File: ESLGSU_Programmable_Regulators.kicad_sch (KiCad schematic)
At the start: 0 parts

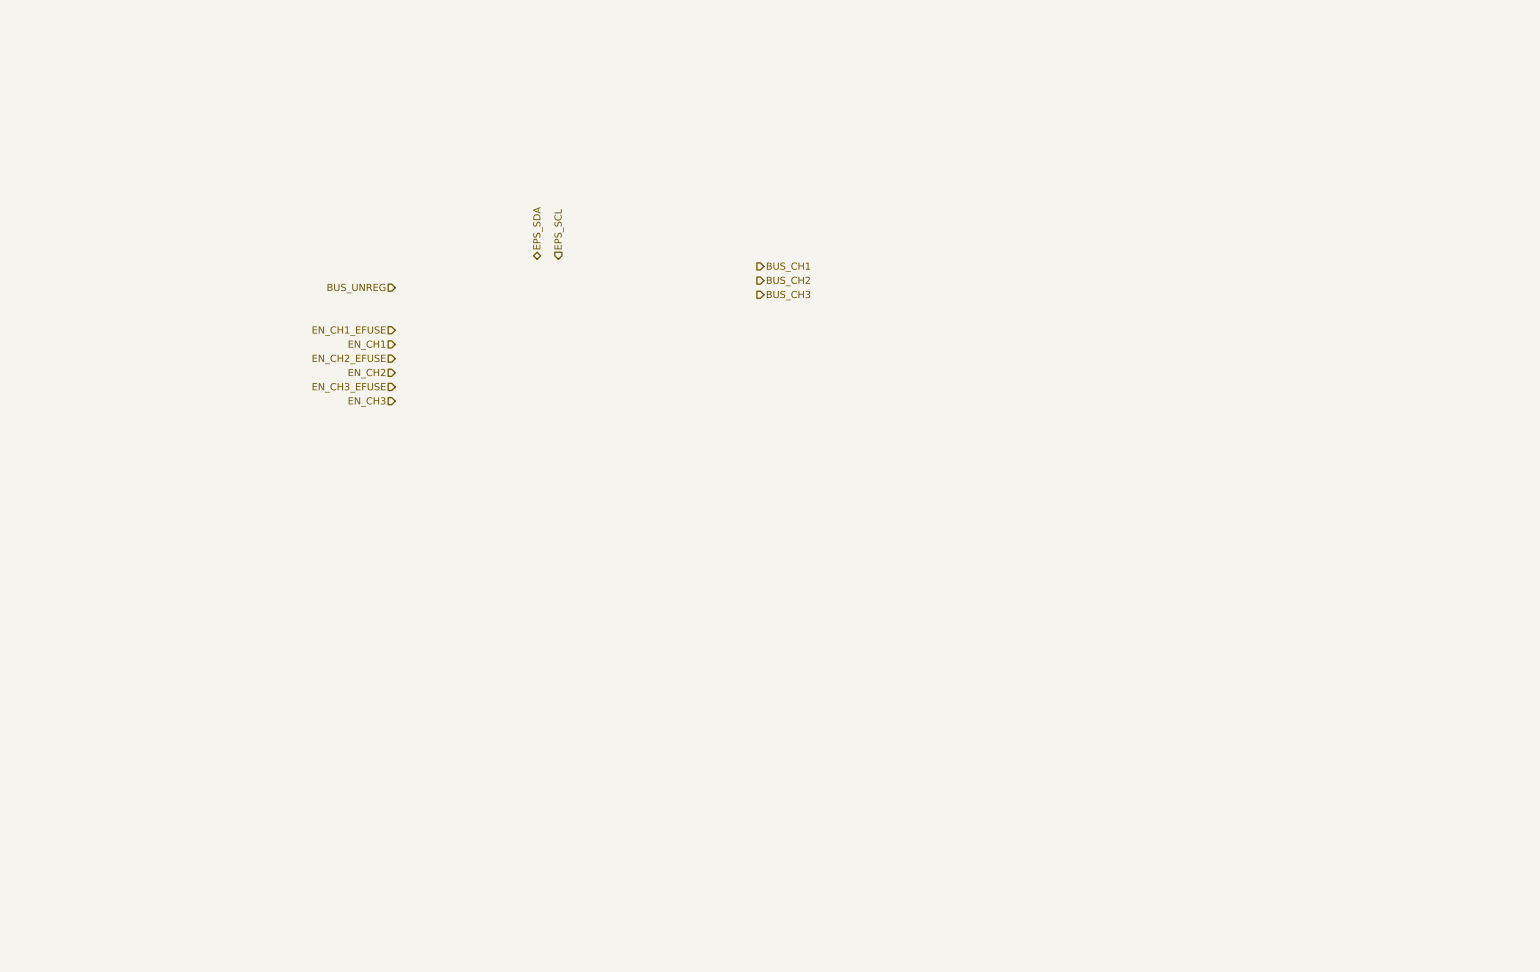
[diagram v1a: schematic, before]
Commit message: Additional power regulation work
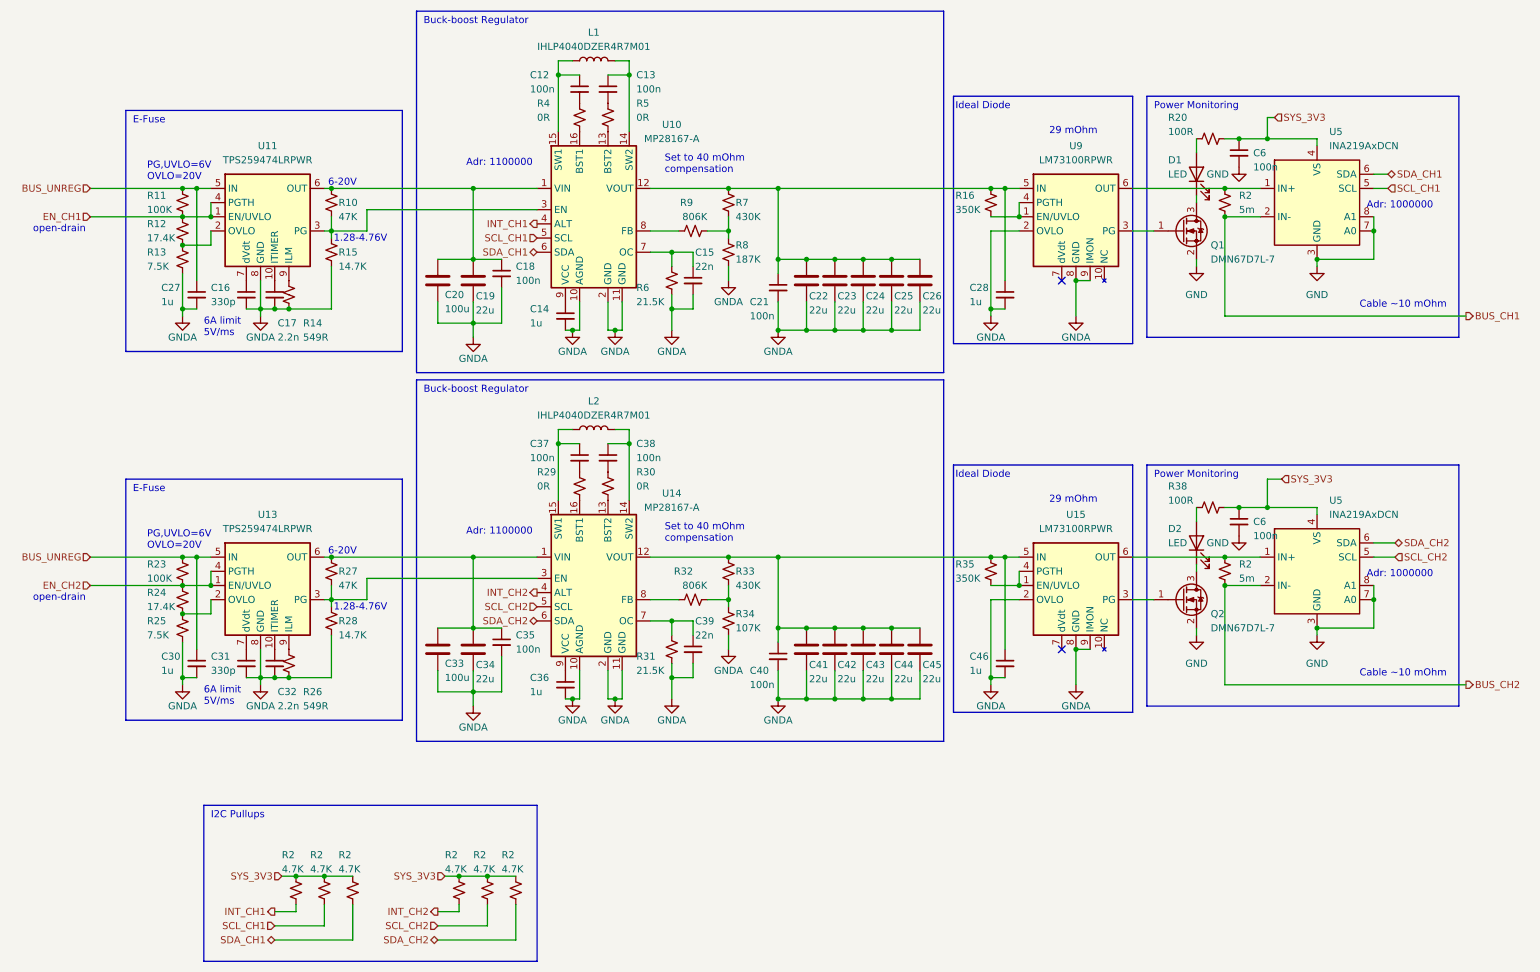
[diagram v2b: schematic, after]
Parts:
- added C12, C13, C18, C21, C35, C37, C38, C40, C6 (x2): 100n, Capacitor_SMD:C_0603_1608Metric, symbol Device:C_Small
- added C14, C27, C28, C30, C36, C46: 1u, Capacitor_SMD:C_0603_1608Metric, symbol Device:C_Small
- added C15, C39: 22n, Capacitor_SMD:C_0603_1608Metric, symbol Device:C_Small
- added C16, C31: 330p, Capacitor_SMD:C_0603_1608Metric, symbol Device:C_Small
- added C17, C32: 2.2n, Capacitor_SMD:C_0603_1608Metric, symbol Device:C_Small
- added C19, C22, C23, C24, C25, C26, C34, C41, C42, C43, C44, C45: 22u, Capacitor_SMD:C_0805_2012Metric, symbol Device:C
- added C20, C33: 100u, Capacitor_SMD:CP_Elec_6.3x7.7, symbol Device:C
- added D1, D2: LED, LED_SMD:LED_0603_1608Metric, symbol Device:LED
- added L1, L2: IHLP4040DZER4R7M01, Inductor_SMD:L_Vishay_IHLP-4040, symbol Device:L
- added Q1, Q2: DMN67D7L-7, Package_TO_SOT_SMD:SOT-323_SC-70, symbol Transistor_FET:DMN67D7L
- added R10, R27: 47K, Resistor_SMD:R_0603_1608Metric, symbol Device:R_Small_US
- added R11, R23: 100K, Resistor_SMD:R_0603_1608Metric, symbol Device:R_Small_US
- added R12, R24: 17.4K, Resistor_SMD:R_0603_1608Metric, symbol Device:R_Small_US
- added R13, R25: 7.5K, Resistor_SMD:R_0603_1608Metric, symbol Device:R_Small_US
- added R14, R26: 549R, Resistor_SMD:R_0603_1608Metric, symbol Device:R_Small_US
- added R15, R28: 14.7K, Resistor_SMD:R_0603_1608Metric, symbol Device:R_Small_US
- added R16, R35: 350K, Resistor_SMD:R_0603_1608Metric, symbol Device:R_Small_US
- added R2 (x2): 5m, Resistor_SMD:R_0603_1608Metric, symbol Device:R_Small_US
- added R2 (x6): 4.7K, Resistor_SMD:R_0603_1608Metric, symbol Device:R_Small_US
- added R20, R38: 100R, Resistor_SMD:R_0603_1608Metric, symbol Device:R_Small_US
- added R29, R30, R4, R5: 0R, Resistor_SMD:R_0603_1608Metric, symbol Device:R_Small_US
- added R31, R6: 21.5K, Resistor_SMD:R_0603_1608Metric, symbol Device:R_Small_US
- added R32, R9: 806K, Resistor_SMD:R_0603_1608Metric, symbol Device:R_Small_US
- added R33, R7: 430K, Resistor_SMD:R_0603_1608Metric, symbol Device:R_Small_US
- added R34: 107K, Resistor_SMD:R_0603_1608Metric, symbol Device:R_Small_US
- added R8: 187K, Resistor_SMD:R_0603_1608Metric, symbol Device:R_Small_US
- added U10, U14: MP28167-A, ESLGSU_Parts_Lib:QFN-16-MP28167, symbol ESLGSU_Parts_Lib:MP28167-A
- added U11, U13: TPS259474LRPWR, ESLGSU_Parts_Lib:VQFN-HR, symbol ESLGSU_Parts_Lib:TPS259474ARPWR
- added U15, U9: LM73100RPWR, ESLGSU_Parts_Lib:VQFN-HR, symbol ESLGSU_Parts_Lib:LM73100
- added U5 (x2): INA219AxDCN, Package_TO_SOT_SMD:SOT-23-8, symbol Sensor_Energy:INA219AxDCN
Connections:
- net BUS_CH1: now also R2.2, U5.2 (IN-)
- net BUS_CH2: now also R2.2, U5.2 (IN-)
- net BUS_UNREG: now also C27.1, C30.1, R11.1, R23.1, U11.5 (IN), U13.5 (IN)
- net EN_CH1: now also R11.2, R12.1, U11.1 (EN/UVLO), U11.4 (PGTH)
- net EN_CH2: now also R23.2, R24.1, U13.1 (EN/UVLO), U13.4 (PGTH)
- new net: D1.1 (K), Q1.3 (D)
- new net: D1.2 (A), R20.2
- new net: C21.1, C22.1, C23.1, C24.1, C25.1, C26.1, C28.1, R16.1, R7.1, U10.12 (VOUT), U9.5 (IN)
- new net: C17.1, U11.10 (ITIMER)
- new net: R12.2, R13.1, U11.2 (OVLO)
- new net: R10.2, R15.1, U10.3 (EN), U11.3 (PG)
- new net: C18.1, C19.1, C20.1, R10.1, U10.1 (VIN), U11.6 (OUT)
- new net: C16.1, U11.7 (dVdt)
- new net: R14.1, U11.9 (ILM)
- new net: C40.1, C41.1, C42.1, C43.1, C44.1, C45.1, C46.1, R33.1, R35.1, U14.12 (VOUT), U15.5 (IN)
- new net: R35.2, U15.1 (EN/UVLO), U15.4 (PGTH)
- new net: Q2.1 (G), U15.3 (PG)
- new net: R2.1, U15.6 (OUT), U5.1 (IN+)
- new net: C33.1, C34.1, C35.1, R27.1, U13.6 (OUT), U14.1 (VIN)
- new net: C38.1, L2.2, U14.14 (SW2)
- new net: C38.2, R30.1
- new net: C14.1, U10.9 (VCC)
- new net: R24.2, R25.1, U13.2 (OVLO)
- new net: R32.2, R33.2, R34.1
- new net: R7.2, R8.1, R9.2
- new net: R27.2, R28.1, U13.3 (PG), U14.3 (EN)
- new net: R16.2, U9.1 (EN/UVLO), U9.4 (PGTH)
- new net: C13.2, R5.1
- new net: R5.2, U10.13 (BST2)
- new net: C13.1, L1.2, U10.14 (SW2)
- new net: C12.1, L1.1, U10.15 (SW1)
- new net: R4.2, U10.16 (BST1)
- new net: C15.1, R6.1, U10.7 (OC)
- new net: R9.1, U10.8 (FB)
- new net: C37.1, L2.1, U14.15 (SW1)
- new net: C37.2, R29.1
- new net: D2.1 (K), Q2.3 (D)
- new net: D2.2 (A), R38.2
- new net: R32.1, U14.8 (FB)
- new net: R26.1, U13.9 (ILM)
- new net: C36.1, U14.9 (VCC)
- new net: C39.1, R31.1, U14.7 (OC)
- new net: R2.1, U5.1 (IN+), U9.6 (OUT)
- new net: R30.2, U14.13 (BST2)
- new net: C32.1, U13.10 (ITIMER)
- new net: R29.2, U14.16 (BST1)
- new net: Q1.1 (G), U9.3 (PG)
- new net: C31.1, U13.7 (dVdt)
- new net: C12.2, R4.1
- new net GND: C6.2, C6.2, Q1.2 (S), Q2.2 (S), U5.3 (GND), U5.3 (GND), U5.7 (A0), U5.7 (A0), U5.8 (A1), U5.8 (A1)
- new net GNDA: C14.2, C15.2, C16.2, C17.2, C18.2, C19.2, C20.2, C21.2, C22.2, C23.2, C24.2, C25.2, C26.2, C27.2, C28.2, C30.2, C31.2, C32.2, C33.2, C34.2, C35.2, C36.2, C39.2, C40.2, C41.2, C42.2, C43.2, C44.2, C45.2, C46.2, R13.2, R14.2, R15.2, R25.2, R26.2, R28.2, R31.2, R34.2, R6.2, R8.2, U10.10 (AGND), U10.11 (GND), U10.2 (GND), U11.8 (GND), U13.8 (GND), U14.10 (AGND), U14.11 (GND), U14.2 (GND), U15.2 (OVLO), U15.8 (GND), U15.9 (IMON), U9.2 (OVLO), U9.8 (GND), U9.9 (IMON)
- new net INT_CH1: R2.2, U10.4 (ALT)
- new net INT_CH2: R2.2, U14.4 (ALT)
- new net SCL_CH1: R2.2, U10.5 (SCL), U5.5 (SCL)
- new net SCL_CH2: R2.2, U14.5 (SCL), U5.5 (SCL)
- new net SDA_CH1: R2.2, U10.6 (SDA), U5.6 (SDA)
- new net SDA_CH2: R2.2, U14.6 (SDA), U5.6 (SDA)
- new net SYS_3V3: C6.1, C6.1, R2.1, R2.1, R2.1, R2.1, R2.1, R2.1, R20.1, R38.1, U5.4 (VS), U5.4 (VS)
- no-connect marks 0 -> 2
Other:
- note added: "1.28-4.76V"
- note added: "29 mOhm"
- note added: "6-20V"
- note added: "6A limit 5V/ms"
- note added: "Adr: 1000000"
- note added: "Adr: 1100000"
- note added: "Buck-boost Regulator"
- note added: "Cable ~10 mOhm"
- note added: "E-Fuse"
- note added: "I2C Pullups"
- note added: "Ideal Diode"
- note added: "PG,UVLO=6V OVLO=20V"
- note added: "Power Monitoring"
- note added: "Set to 40 mOhm compensation"
- note added: "open-drain"

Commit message: Added 5v/3V3 regulators and mux
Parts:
- added R87 (x2): 47K, Resistor_SMD:R_0603_1608Metric, symbol Device:R_Small_US
- added TP1 (x6): TestPoint, TestPoint:TestPoint_Pad_D2.0mm, symbol Connector:TestPoint
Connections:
- net BUS_CH1: now also TP1.1
- net BUS_CH2: now also TP1.1
- net at D1.2 (A), R20.2: now also R87.1
- net at C21.1, C22.1, C23.1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: now also TP1.1
- net at C18.1, C19.1, C20.1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: now also TP1.1
- net at C40.1, C41.1, C42.1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: now also TP1.1
- net at Q2.1 (G), U15.3 (PG): now also R87.2
- net at C33.1, C34.1, C35.1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: now also TP1.1
- net at D2.2 (A), R38.2: now also R87.1
- net at Q1.1 (G), U9.3 (PG): now also R87.2

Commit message: uC Interface work
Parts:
- Q1, Q2: footprint Package_TO_SOT_SMD:SOT-323_SC-70 -> Package_TO_SOT_SMD:SOT-23
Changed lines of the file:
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@@
     )
   )
-  (symbol (lib_id "ESLGSU_Parts_Lib:LM73100") (at 203.2 121.92 0) (unit 1)
+  (symbol (lib_id "ESLGSU_Parts_Lib:LM73100") (at 203.2 120.65 0) (unit 1)
     (in_bom yes) (on_board yes) (dnp no) (fields_autoplaced)
-    (property "Reference" "U15" (at 203.2 109.22 0)
-      (effects (font (size 1.27 1.27)))
-    )
-    (property "Value" "LM73100RPWR" (at 203.2 111.76 0)
-      (effects (font (size 1.27 1.27)))
-    )
-    (property "Footprint" "ESLGSU_Parts_Lib:VQFN-HR" (at 201.93 140.97 0)
-      (effects (font (size 1.27 1.27)) hide)
-    )
-    (property "Datasheet" "" (at 203.2 121.92 0)
+    (property "Reference" "U15" (at 203.2 107.95 0)
+      (effects (font (size 1.27 1.27)))
+    )
+    (property "Value" "LM73100RPWR" (at 203.2 110.49 0)
+      (effects (font (size 1.27 1.27)))
+    )
+    (property "Footprint" "ESLGSU_Parts_Lib:VQFN-HR" (at 201.93 139.7 0)
+      (effects (font (size 1.27 1.27)) hide)
+    )
+    (property "Datasheet" "" (at 203.2 120.65 0)
       (effects (font (size 1.27 1.27)) hide)
     )
@@
       (effects (font (size 1.27 1.27)) (justify left))
     )
-    (property "Footprint" "Package_TO_SOT_SMD:SOT-323_SC-70" (at 227.33 126.365 0)
+    (property "Footprint" "Package_TO_SOT_SMD:SOT-23" (at 227.33 126.365 0)
       (effects (font (size 1.27 1.27) italic) (justify left) hide)
     )
@@
       (effects (font (size 1.27 1.27)) (justify left))
     )
-    (property "Footprint" "Package_TO_SOT_SMD:SOT-323_SC-70" (at 227.33 60.325 0)
+    (property "Footprint" "Package_TO_SOT_SMD:SOT-23" (at 227.33 60.325 0)
       (effects (font (size 1.27 1.27) italic) (justify left) hide)
     )
@@
     )
   )
-  (symbol (lib_id "ESLGSU_Parts_Lib:LM73100") (at 203.2 55.88 0) (unit 1)
+  (symbol (lib_id "ESLGSU_Parts_Lib:LM73100") (at 203.2 54.61 0) (unit 1)
     (in_bom yes) (on_board yes) (dnp no) (fields_autoplaced)
-    (property "Reference" "U9" (at 203.2 43.18 0)
-      (effects (font (size 1.27 1.27)))
-    )
-    (property "Value" "LM73100RPWR" (at 203.2 45.72 0)
-      (effects (font (size 1.27 1.27)))
-    )
-    (property "Footprint" "ESLGSU_Parts_Lib:VQFN-HR" (at 201.93 74.93 0)
-      (effects (font (size 1.27 1.27)) hide)
-    )
-    (property "Datasheet" "" (at 203.2 55.88 0)
-      (effects (font (size 1.27 1.27)) hide)
-    )
+    (property "Reference" "U9" (at 203.2 41.91 0)
+      (effects (font (size 1.27 1.27)))
+    )
+    (property "Value" "LM73100RPWR" (at 203.2 44.45 0)
+      (effects (font (size 1.27 1.27)))
+    )
+    (property "Footprint" "ESLGSU_Parts_Lib:VQFN-HR" (at 201.93 73.66 0)
+      (effects (font (size 1.27 1.27)) hide)
+    )
+    (property "Datasheet" "" (at 203.2 54.61 0)
+      (effects (font (size 1.27 1.27)) hide)
+    )

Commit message: Finished interfaces work
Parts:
- C12, C13, C14, C15, C16, C17, C18, C21, C27, C28, C30, C31, C32, C35, C36, C37, C38, C39, C40, C46, C6: footprint Capacitor_SMD:C_0603_1608Metric -> Capacitor_SMD:C_0402_1005Metric
- R10, R11, R12, R13, R14, R15, R16, R2, R20, R23, R24, R25, R26, R27, R28, R29, R30, R31, R32, R33, R34, R35, R38, R4, R5, R6, R7, R8, R87, R9: footprint Resistor_SMD:R_0603_1608Metric -> Resistor_SMD:R_0402_1005Metric

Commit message: More PCB work
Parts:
- TP1: footprint TestPoint:TestPoint_Pad_D2.0mm -> TestPoint:TestPoint_Pad_D1.5mm
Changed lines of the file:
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@@
       (effects (font (size 1.27 1.27)) (justify left))
     )
-    (property "Footprint" "TestPoint:TestPoint_Pad_D2.0mm" (at 237.49 73.66 0)
+    (property "Footprint" "TestPoint:TestPoint_Pad_D1.5mm" (at 237.49 73.66 0)
       (effects (font (size 1.27 1.27)) hide)
     )
@@
       (effects (font (size 1.27 1.27)) (justify left))
     )
-    (property "Footprint" "TestPoint:TestPoint_Pad_D2.0mm" (at 154.94 116.84 0)
+    (property "Footprint" "TestPoint:TestPoint_Pad_D1.5mm" (at 154.94 116.84 0)
       (effects (font (size 1.27 1.27)) hide)
     )
@@
       (effects (font (size 1.27 1.27)) (justify left))
     )
-    (property "Footprint" "TestPoint:TestPoint_Pad_D2.0mm" (at 154.94 50.8 0)
+    (property "Footprint" "TestPoint:TestPoint_Pad_D1.5mm" (at 154.94 50.8 0)
       (effects (font (size 1.27 1.27)) hide)
     )
@@
       (effects (font (size 1.27 1.27)) (justify left))
     )
-    (property "Footprint" "TestPoint:TestPoint_Pad_D2.0mm" (at 237.49 139.7 0)
+    (property "Footprint" "TestPoint:TestPoint_Pad_D1.5mm" (at 237.49 139.7 0)
       (effects (font (size 1.27 1.27)) hide)
     )
@@
       (effects (font (size 1.27 1.27)) (justify left))
     )
-    (property "Footprint" "TestPoint:TestPoint_Pad_D2.0mm" (at 91.44 50.8 0)
+    (property "Footprint" "TestPoint:TestPoint_Pad_D1.5mm" (at 91.44 50.8 0)
       (effects (font (size 1.27 1.27)) hide)
     )
@@
       (effects (font (size 1.27 1.27)) (justify left))
     )
-    (property "Footprint" "TestPoint:TestPoint_Pad_D2.0mm" (at 91.44 116.84 0)
-      (effects (font (size 1.27 1.27)) hide)
-    )
+    (property "Footprint" "TestPoint:TestPoint_Pad_D1.5mm" (at 91.44 116.84 0)
+      (effects (font (size 1.27 1.27)) hide)
+    )

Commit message: Tried to prepare for order
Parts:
- D1, D2: value LED -> TZ-P2-0603GTCS1-0.6T
- U5: value INA219AxDCN -> INA219AIDCNR
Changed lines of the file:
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@@
       (effects (font (size 1.27 1.27)) (justify right))
     )
-    (property "Value" "LED" (at 219.71 48.26 90)
+    (property "Value" "TZ-P2-0603GTCS1-0.6T" (at 219.71 48.26 90)
       (effects (font (size 1.27 1.27)) (justify right))
     )
@@
       (effects (font (size 1.27 1.27)) (justify right))
     )
-    (property "Value" "LED" (at 219.71 114.3 90)
+    (property "Value" "TZ-P2-0603GTCS1-0.6T" (at 219.71 114.3 90)
       (effects (font (size 1.27 1.27)) (justify right))
     )
@@
       (effects (font (size 1.27 1.27)) (justify left))
     )
-    (property "Value" "INA219AxDCN" (at 248.5741 109.22 0)
+    (property "Value" "INA219AIDCNR" (at 248.5741 109.22 0)
       (effects (font (size 1.27 1.27)) (justify left))
     )
@@
       (effects (font (size 1.27 1.27)) (justify left))
     )
-    (property "Value" "INA219AxDCN" (at 248.5741 43.18 0)
-      (effects (font (size 1.27 1.27)) (justify left))
-    )
+    (property "Value" "INA219AIDCNR" (at 248.5741 43.18 0)
+      (effects (font (size 1.27 1.27)) (justify left))
+    )
